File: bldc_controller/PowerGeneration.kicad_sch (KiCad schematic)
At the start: 78 parts, among them U12 LMR36006FSCQRNXRQ1, U2 MAX15062BATA+T, U3 ADP5301ACBZ-4-R7, U4 LP2992IM5-3.3/NOPB

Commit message: minor changes before changing mcu
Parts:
- added NT2: FB_12V, 0_net_tie:NetTie-2_SMD_Pad0.2mm, symbol Device:NetTie_2
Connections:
- net +12V: now also NT2.2; no longer R46.1
- net FB_12V: now also R46.1, NT2.1; no longer R46.2, R47.1, U12.7 (FB)
- new net FB_DIV_12V: R46.2, R47.1, U12.7 (FB)
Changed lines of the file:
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@@
     (stroke (width 0.381) (type default) (color 200 50 50 1))
+  )
+  (wire (pts (xy 149.86 80.01) (xy 149.86 77.47))
+    (stroke (width 0) (type default))
   )
   (wire (pts (xy 248.92 45.72) (xy 240.03 45.72))
@@
     (stroke (width 0.381) (type default) (color 200 50 50 1))
   )
-  (wire (pts (xy 149.86 87.63) (xy 149.86 77.47))
+  (wire (pts (xy 149.86 87.63) (xy 149.86 85.09))
     (stroke (width 0) (type default))
   )
@@
     (effects (font (size 1.524 1.524) (color 0 0 0 1)) (justify left top))
   )
+  (label "FB_12V" (at 149.86 87.63 0) (fields_autoplaced)
+    (effects (font (size 1.27 1.27)) (justify left bottom))
+  )
   (label "FB_3V3" (at 240.03 38.1 0) (fields_autoplaced)
     (effects (font (size 1.27 1.27)) (justify left bottom))
@@
     (effects (font (size 1.27 1.27)) (justify right bottom))
   )
-  (label "FB_12V" (at 127 97.79 0) (fields_autoplaced)
+  (label "FB_DIV_12V" (at 127 97.79 0) (fields_autoplaced)
     (effects (font (size 1.27 1.27)) (justify left bottom))
   )
@@
         )
       )
+    )
+  )
+  (symbol (lib_id "Device:NetTie_2") (at 149.86 82.55 90) (unit 1)
+    (in_bom no) (on_board yes) (dnp no)
+    (property "Reference" "NT2" (at 151.13 83.82 90)
+      (effects (font (size 1.27 1.27)) (justify right))
+    )
+    (property "Value" "FB_12V" (at 151.13 81.28 90)
+      (effects (font (size 1.27 1.27)) (justify right))
+    )
+    (property "Footprint" "0_net_tie:NetTie-2_SMD_Pad0.2mm" (at 149.86 82.55 0)
+      (effects (font (size 1.27 1.27)) hide)
+    )
+    (property "Datasheet" "~" (at 149.86 82.55 0)
+      (effects (font (size 1.27 1.27)) hide)
+    )
+    (pin "1")
+    (pin "2")
+    (instances
+      (project "bldc_controller"
+        (path "/0650c7a8-acba-429c-9f8e-eec0baf0bc1c/b89a7d22-bda3-4776-b5ce-8f6b0eb8f2a5"
+          (reference "NT2") (unit 1)
+        )
+      )

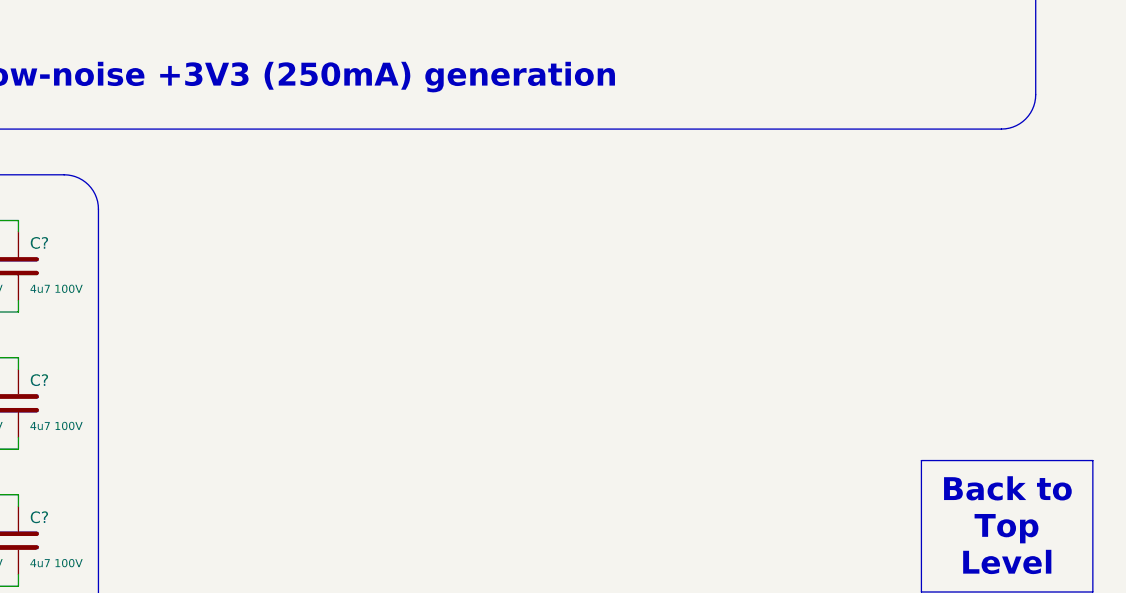
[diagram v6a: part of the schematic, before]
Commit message: Added TVS diodes to all interfaces
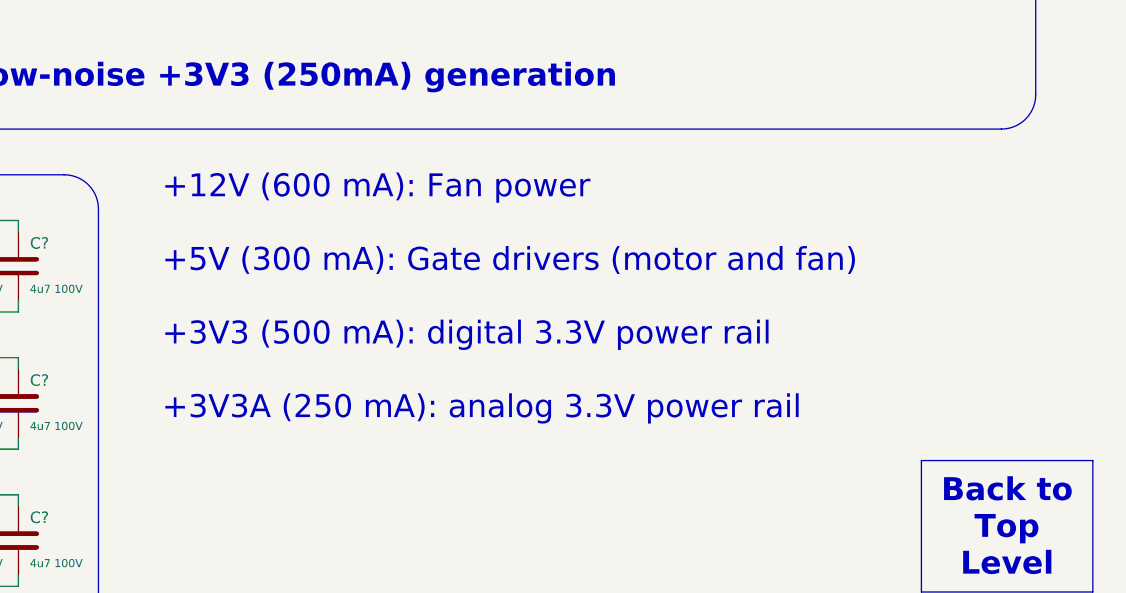
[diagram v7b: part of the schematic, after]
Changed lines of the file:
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@@
     (effects (font (size 2.54 2.54) (thickness 0.508) bold (color 0 0 0 1)) (href "#1"))
+  )
+  (text_box "+12V (600 mA): Fan power\n\n+5V (300 mA): Gate drivers (motor and fan)\n\n+3V3 (500 mA): digital 3.3V power rail\n\n+3V3A (250 mA): analog 3.3V power rail\n"
+    (at 179.07 133.35 0) (size 99.06 30.48)
+    (stroke (width -0.0001) (type default))
+    (fill (type none))
+    (effects (font (size 2.54 2.54) (color 0 0 0 1)) (justify left bottom))
   )
   (text_box "Regulators for +5V (300mA), +3V3 (500mA) and low-noise +3V3 (250mA) generation"

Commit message: might have fixed net issue, added dxf and svgs
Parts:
- gave numbers to parts that had none: 52
- renumbered C86 to C110, C86 to C111, C65 to C114
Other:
- moved on the sheet: C1, C10, C108, C109, C11, C110, C111, C112, C113, C114, C115, C12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
